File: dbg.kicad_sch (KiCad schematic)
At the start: 22 parts, among them J18 USB_C_Receptacle_USB2.0_16P, J19 Conn_02x05_Odd_Even, SW2 SKRPANE010, U18 STM32F103C8Tx, U19 USBLC6-2SC6, Y2 8 MHz

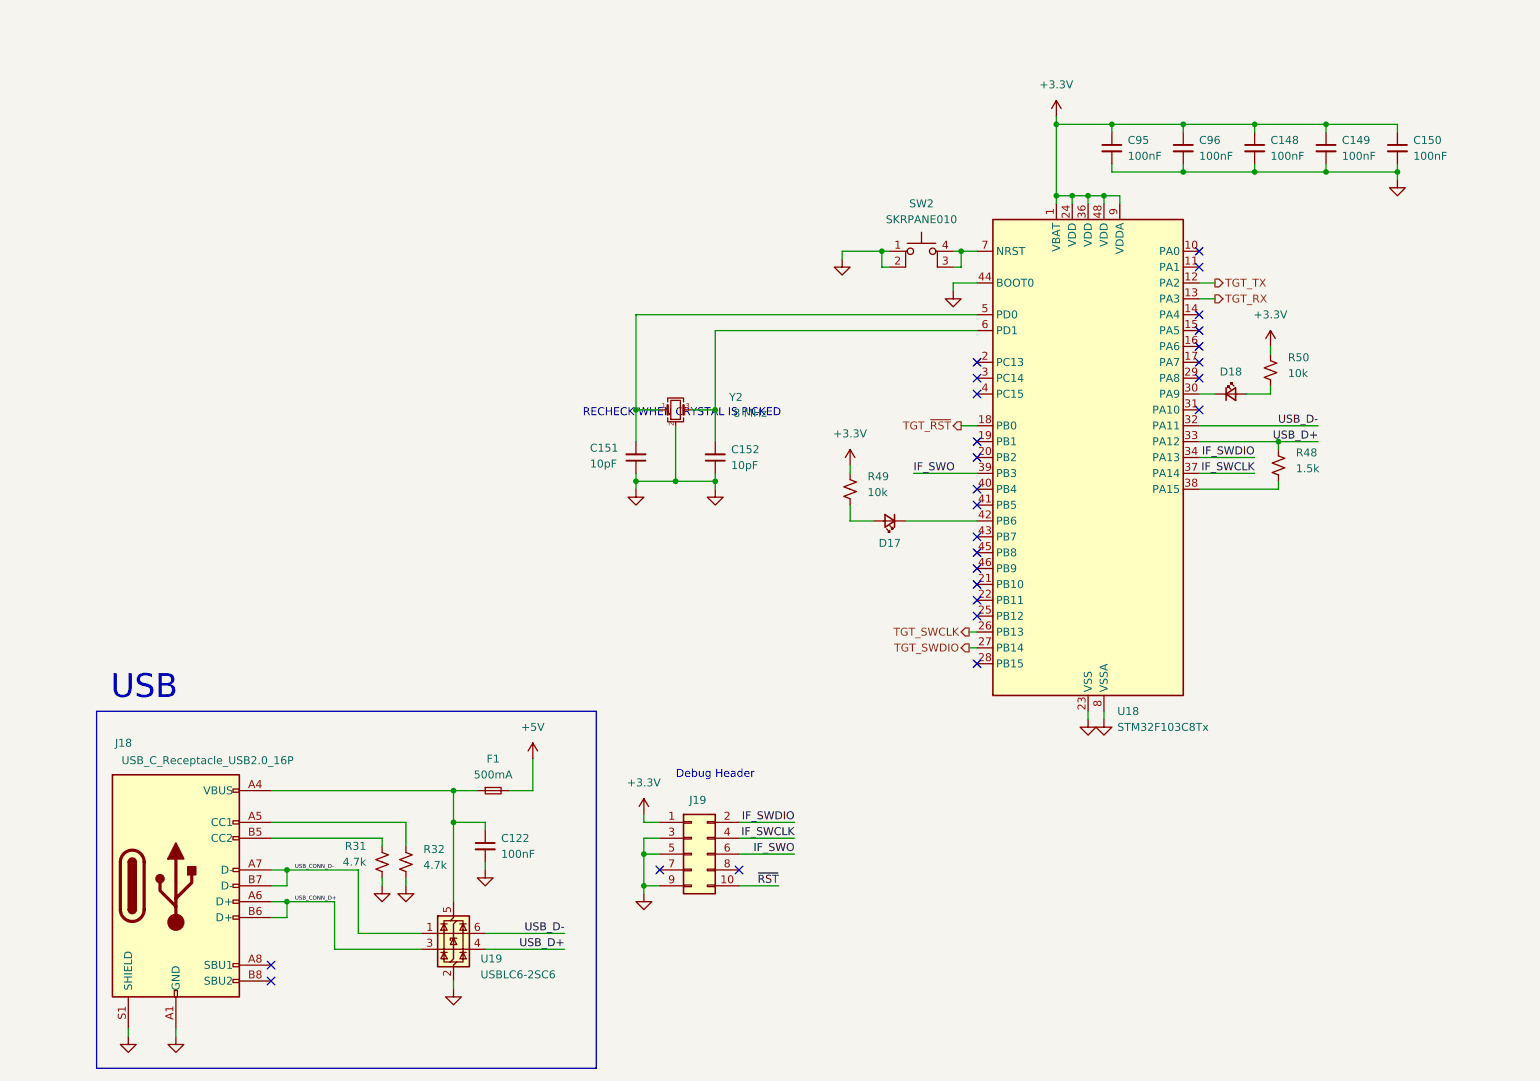
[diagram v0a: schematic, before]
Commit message: Soften scope, begin layout, reorganize sheets (still need to delete extras)
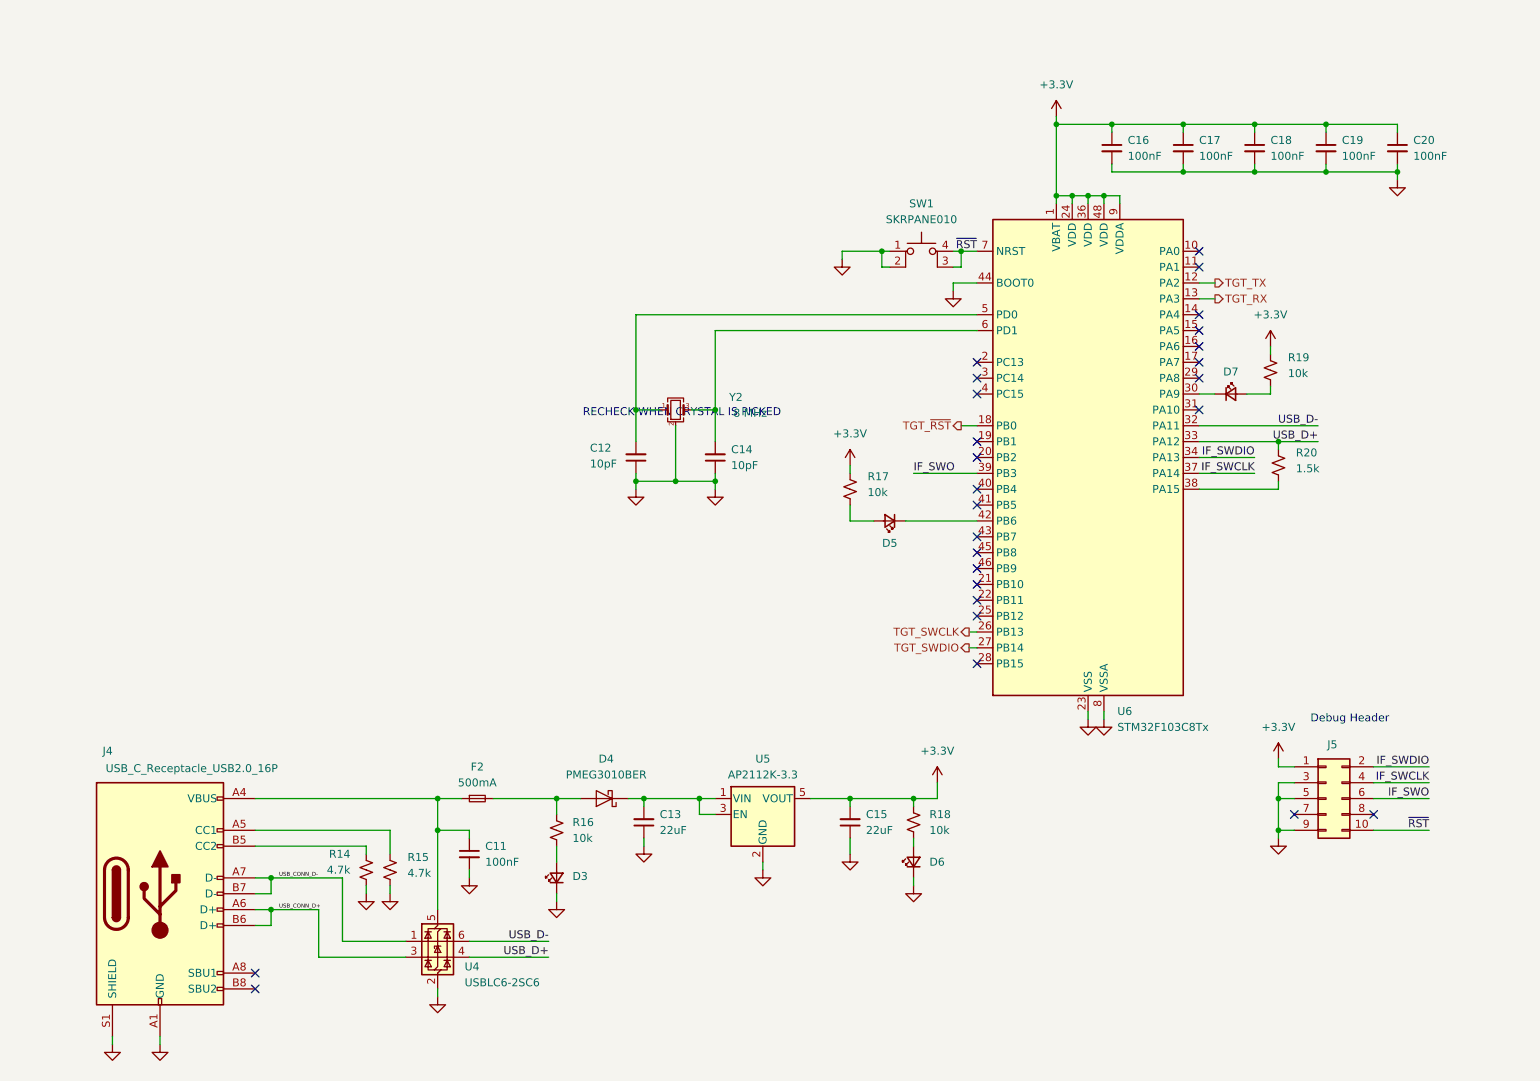
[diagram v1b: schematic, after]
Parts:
- added C13, C15: 22uF, APRLPrints:C_0805, symbol Device:C_Small
- added D3, D6: LED_Small, APRLPrints:LED_0603, symbol Device:LED_Small
- added D4: PMEG3010BER, Diode_SMD:Nexperia_CFP3_SOD-123W, symbol Diode:PMEG3010BER
- added R16, R18: 10k, APRLPrints:R_0603, symbol Device:R_Small_US
- added U5: AP2112K-3.3, Package_TO_SOT_SMD:SOT-23-5, symbol Regulator_Linear:AP2112K-3.3
- C11: renamed from C122; footprint aprlprints:C_0603-noct -> APRLPrints:C_0603
- C12: renamed from C151; footprint (none) -> APRLPrints:C_0603
- C14: renamed from C152; footprint (none) -> APRLPrints:C_0603
- C16: renamed from C95; footprint (none) -> APRLPrints:C_0603
- C17: renamed from C96; footprint (none) -> APRLPrints:C_0603
- C18: renamed from C148; footprint (none) -> APRLPrints:C_0603
- C19: renamed from C149; footprint (none) -> APRLPrints:C_0603
- C20: renamed from C150; footprint (none) -> APRLPrints:C_0603
- D5: renamed from D17; footprint (none) -> APRLPrints:LED_0603
- D7: renamed from D18; footprint (none) -> APRLPrints:LED_0603
- R14: renamed from R31; footprint aprlprints:R_0603-noct -> APRLPrints:R_0603
- R15: renamed from R32; footprint aprlprints:R_0603-noct -> APRLPrints:R_0603
- R17: renamed from R49; footprint aprlprints:R_0603-noct -> APRLPrints:R_0603
- R19: renamed from R50; footprint aprlprints:R_0603-noct -> APRLPrints:R_0603
- R20: renamed from R48; footprint aprlprints:R_0603-noct -> APRLPrints:R_0603
- SW1: renamed from SW2; footprint (none) -> APRLPrints:SKRPANE010
- Y2: footprint (none) -> APRLPrints:3225-4P-L; private KLC_S4.1 -> (none)
- renumbered F1 to F2, J18 to J4, J19 to J5, U19 to U4, U18 to U6
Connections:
- net +3.3V: now also C15.2, R18.1, U5.5 (VOUT)
- net GND: now also C13.1, C15.1, D3.1 (K), D6.1 (K), U5.2 (GND)
- net ~{RST}: now also SW1.3 (K), SW1.4 (A), U6.7 (NRST)
- net +5V: no longer names the net of F2.2
- net +5V: now also D4.2 (A), R16.1
- new net: D6.2 (A), R18.2
- new net: D3.2 (A), R16.2
- new net: C13.2, D4.1 (K), U5.1 (VIN), U5.3 (EN)
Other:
- note removed: "USB"
- moved on the sheet: C11, F2, J4, J5, R14, R15, U4

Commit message: ???
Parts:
- removed C12, C14: 10pF, APRLPrints:C_0603, symbol Device:C_Small
- removed C13, C15: 22uF, APRLPrints:C_0805, symbol Device:C_Small
- removed C16, C17, C18: 100nF, APRLPrints:C_0603, symbol Device:C_Small
- removed D4: PMEG3010BER, Diode_SMD:Nexperia_CFP3_SOD-123W, symbol Diode:PMEG3010BER
- removed D6, D7: LED_Small, APRLPrints:LED_0603, symbol Device:LED_Small
- removed F2: 500mA, Fuse:Fuse_0805_2012Metric, symbol Device:Fuse_Small
- removed R18, R19: 10k, APRLPrints:R_0603, symbol Device:R_Small_US
- removed R20: 1.5k, APRLPrints:R_0603, symbol Device:R_Small_US
- removed U5: AP2112K-3.3, Package_TO_SOT_SMD:SOT-23-5, symbol Regulator_Linear:AP2112K-3.3
- removed U6: STM32F103C8Tx, Package_QFP:LQFP-48_7x7mm_P0.5mm, symbol MCU_ST_STM32F1:STM32F103C8Tx
- removed Y2: 8 MHz, APRLPrints:3225-4P-L, symbol Device:Crystal_GND24_Small
- added C23: 100nF, APRLPrints:C_0603, symbol Device:C_Small
- added D1, D4: LED_Small, APRLPrints:LED_0603, symbol Device:LED_Small
- added D2: PMEG3010BER, Diode_SMD:Nexperia_CFP3_SOD-123W, symbol Diode:PMEG3010BER
- added F1: 500mA, Fuse:Fuse_0805_2012Metric, symbol Device:Fuse_Small
- added J12: USB_C_Receptacle_USB2.0_16P, Connector_USB:USB_C_Receptacle_HRO_TYPE-C-31-M-12, symbol Connector:USB_C_Receptacle_USB2.0_16P
- added R10, R12: 4.7k, APRLPrints:R_0603, symbol Device:R_Small_US
- added R14, R15: 10k, APRLPrints:R_0603, symbol Device:R_Small_US
- added U10: USBLC6-2SC6, Package_TO_SOT_SMD:SOT-23-6, symbol Power_Protection:USBLC6-2SC6
- added U12: STM32F042F4Px, Package_SO:TSSOP-20_4.4x6.5mm_P0.65mm, symbol MCU_ST_STM32F0:STM32F042F4Px
- renumbered C11 to C24, C19 to C25, C20 to C26, J4 to J13, J5 to J14, R14 to R11, R15 to R13, U4 to U11
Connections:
- net +3.3V: now also D3.2 (A), D5.2 (A), D4.2 (A), U12.16 (VDD), U12.5 (VDDA); no longer R17.1
- net GND: now also C23.2, D1.1 (K), J12.A1 (GND), J12.A12 (GND), J12.B1 (GND), J12.B12 (GND), J12.S1 (SHIELD), R10.1, R12.2, U10.2 (GND), U12.1 (PB8), U12.15 (VSSA); no longer D3.1 (K)
- net IF_SWCLK: now also U12.20 (PA14)
- net IF_SWDIO: now also U12.19 (PA13)
- net IF_SWO: now also U12.8 (PA2)
- net TGT_SWCLK: now also U12.12 (PA6)
- net TGT_SWDIO: now also U12.11 (PA5)
- net USB_CONN_D+: now also J12.A6 (D+), J12.B6 (D+), U10.3 (I/O2)
- net USB_CONN_D-: now also J12.A7 (D-), J12.B7 (D-), U10.1 (I/O1)
- net USB_D+: now also U10.4 (I/O2), U12.18 (PA10/PA12)
- net USB_D-: now also U10.6 (I/O1), U12.17 (PA9/PA11)
- net ~{RST}: now also U12.4 (NRST)
- net at R17.2: now also U12.10 (PA4); no longer D5.2 (A)
- net at R16.1: now also D4.1 (K)
- net at R16.2: now also U12.7 (PA1); no longer D3.2 (A)
- net at D5.1 (K): now also R17.1
- new net: J12.A5 (CC1), R12.1
- new net: D3.1 (K), R15.1
- new net: C23.1, F1.1, J12.A4 (VBUS), J12.A9 (VBUS), J12.B4 (VBUS), J12.B9 (VBUS), U10.5 (VBUS)
- new net: J12.B5 (CC2), R10.2
- new net: R15.2, U12.6 (PA0)
- new net: D2.2 (A), F1.2, R14.1
- new net: D1.2 (A), R14.2
- new net +5V: D2.1 (K)
- new net TGT_RST: U12.14 (PB1)
- new net TGT_SWO: U12.13 (PA7)
- no-connect marks 26 -> 9
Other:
- note added: "Debugger Microcontroller USB"
- note added: "Integrated dap42 Debugger"
- note added: "Main Microcontroller USB"
- note added: "May change IF_SWO"
- note added: "On-Board Debugger (dap42)"
- note removed: "RECHECK WHEN CRYSTAL IS PICKED"
- moved on the sheet: C24, C25, C26, J13, J14, R11, R13, U11

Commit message: loadcell math coming soon(tm)
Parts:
- renumbered C25 to C28, C26 to C29, C23 to C30, C24 to C31, D2 to D1, D1 to D2, J12 to J11, J13 to J12, J14 to J13, R14 to R22, R10 to R23, R12 to R24, R15 to R25, R16 to R26, R17 to R27, R11 to R28, R13 to R29, SW1 to SW2, U12 to U10, U10 to U9
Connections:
- net USB_D+: no longer U9.4 (I/O2)
- net USB_D-: no longer U9.6 (I/O1)
- net IF_SWO: no longer names the net of U10.8 (PA2)
- net IF_SWO: no longer J13.6 (Pin_6)
- new net MCU_USB_D+: U9.4 (I/O2)
- new net MCU_USB_D-: U9.6 (I/O1)
- no-connect marks 9 -> 11
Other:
- note added: "Debug USB"
- note added: "PA2 and PA3 are TGT_RX and TGT_TX typically"
- note removed: "Debugger Microcontroller USB"
- note removed: "May change IF_SWO"

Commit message: a
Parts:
- removed J13: Conn_02x05_Odd_Even, Connector_PinHeader_2.54mm:PinHeader_2x05_P2.54mm_Vertical, symbol Connector_Generic:Conn_02x05_Odd_Even
- added J9: Conn_ARM_SWD_TagConnect_TC2030-NL, Connector:Tag-Connect_TC2030-IDC-NL_2x03_P1.27mm_Vertical, symbol Connector:Conn_ARM_SWD_TagConnect_TC2030-NL
- J7: renamed from J11; footprint Connector_USB:USB_C_Receptacle_HRO_TYPE-C-31-M-12 -> libserie:USB_C_Receptacle_HRO_TYPE-C-31-M-12
- J8: renamed from J12; footprint Connector_USB:USB_C_Receptacle_HRO_TYPE-C-31-M-12 -> libserie:USB_C_Receptacle_HRO_TYPE-C-31-M-12
- renumbered C28 to C24, C29 to C25, C30 to C26, C31 to C27, R22 to R15, R23 to R16, R24 to R17, R25 to R18, R26 to R19, R27 to R20, R28 to R21, R29 to R22, U11 to U10, U9 to U8, U10 to U9
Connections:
- net +3.3V: now also J9.1 (VCC)
- net GND: now also J9.5 (GND)
- net IF_SWCLK: now also J9.4 (SWCLK)
- net IF_SWDIO: now also J9.2 (SWDIO)
- net ~{RST}: now also J9.3 (~{RESET})
- net TGT_SWO: no longer names the net of U9.13 (PA7)
- no-connect marks 11 -> 10
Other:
- moved on the sheet: C24, C25, D3, D4, D5, R18, R19, R20, SW2, U9
